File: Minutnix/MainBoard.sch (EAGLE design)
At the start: 134 parts, among them IC1 MEGA8-AI, IC6 TP4056, IC7 FT232RL, IC9 SC4503, Q4 32.768kHz, T1 DMN3024LSD, X1 FH12-12S-0.5SH, X2 JST-XH-03-PIN-LONG-PAD, X4 JST-XH-03-PIN-LONG-PAD

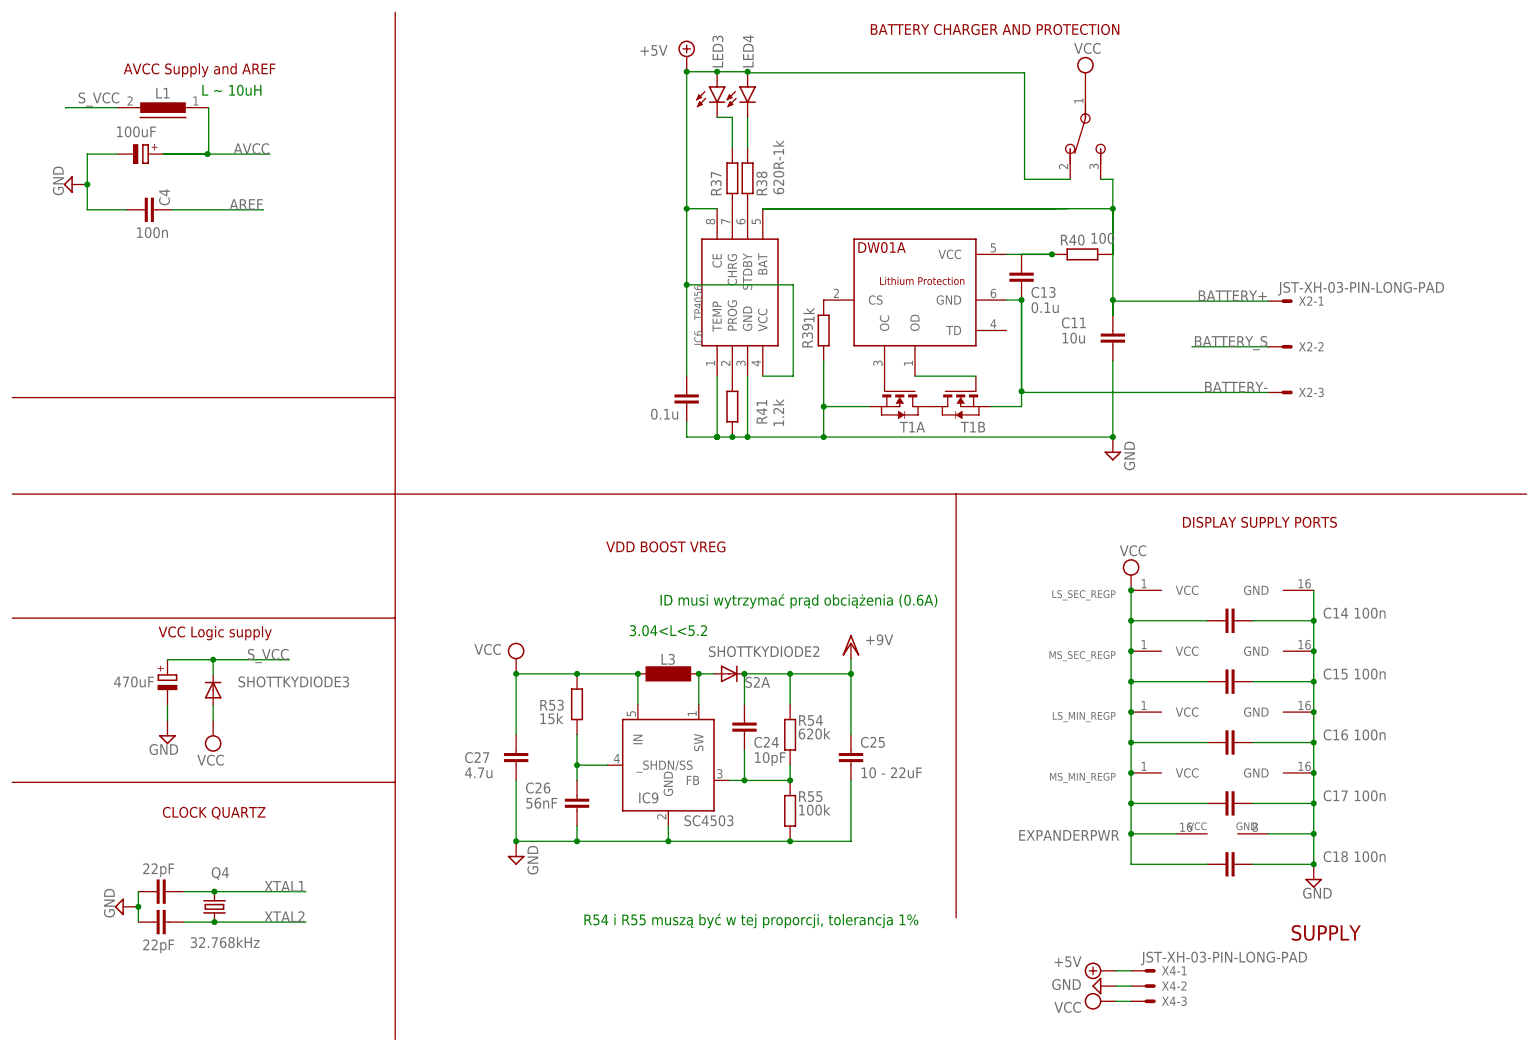
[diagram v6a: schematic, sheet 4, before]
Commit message: Supply replacements + corrections
Vreg replaced by pololu board
Added LDO for VCC supply and moved power on switch
Protection included into battery cicruit
Corrected supply of ft232 diodes
Changed supply of photoresistor to avcc
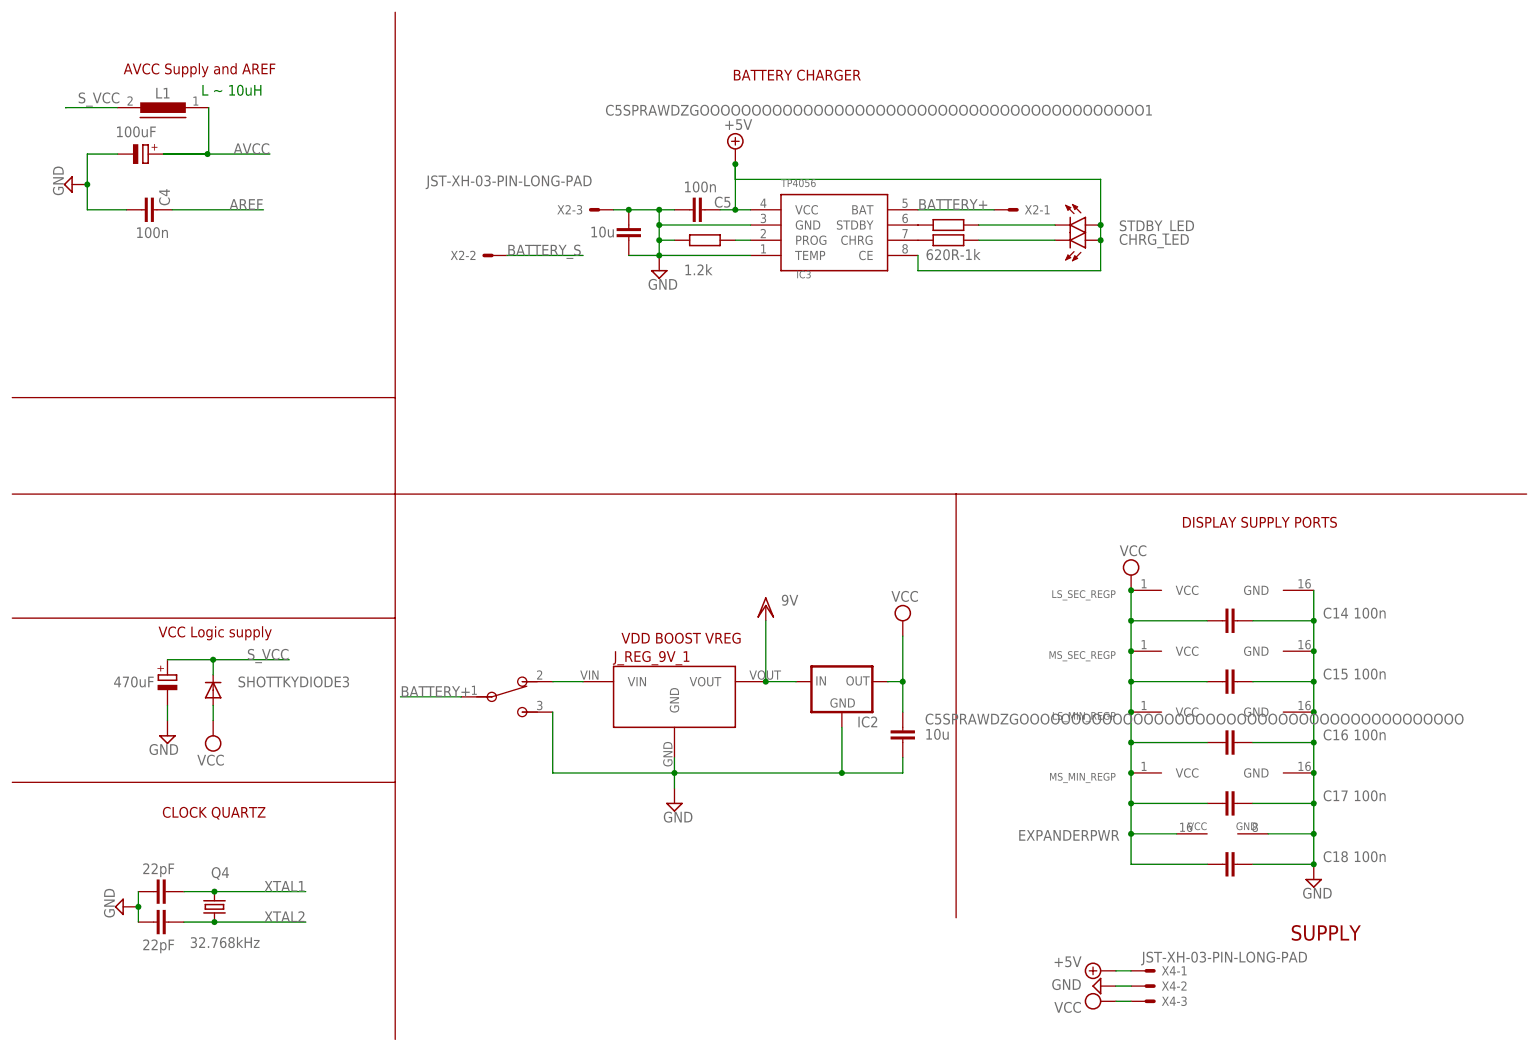
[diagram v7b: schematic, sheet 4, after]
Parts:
- removed C11: 10u, capacitor-wima:C2.5/2
- removed C12, C13: 0.1u, capacitor-wima:C2.5/2
- removed C24: 10pF, capacitor-wima:C2.5/2
- removed C25: 10 - 22uF, capacitor-wima:C2.5/2
- removed C26: 56nF, capacitor-wima:C2.5/2
- removed C27: 4.7u, capacitor-wima:C2.5/2
- removed IC6: TP4056, TP4056:TP4056
- removed IC9: SC4503, v-reg-3:SC4503
- removed L3: 4.237H, inductor-neosid:MS42
- removed LED3, LED4: (no value), led:LEDCHIPLED_0603
- removed R37: 620R-1K, rcl:R-EU_R1206
- removed R38: 620R-1k, rcl:R-EU_R1206
- removed R41: 1.2k, rcl:R-EU_R1206
- removed R53: 15k, rcl:R-EU_R1206
- removed R54: 620k, rcl:R-EU_R1206
- removed R55: 100k, rcl:R-EU_R1206
- removed SHOTTKYDIODE2: S2A, s2x_10:S2A
- removed T1: DMN3024LSD, FS8205A:DMN3024LSD
- removed U$2: DW01A, DW01A:DW01A
- added C5: 100n, rcl:C-EUC0603
- added C5SPRAWDZGOOOOOOOOOOOOOOOOOOOOOOOOOOOOOOOOOOOOOOOOOOO, C5SPRAWDZGOOOOOOOOOOOOOOOOOOOOOOOOOOOOOOOOOOOOOOOOOOO1: 10u, rcl:C-EUC3216
- added CHRG_LED, STDBY_LED: (no value), led:LEDCHIPLED_0603
- added IC2: (no value), v-reg-2:LM1117
- added IC3: TP4056, TP4056:TP4056
- added J_REG_9V_1: 9V_VOLTAGE_REGULATOR, Pololu_vreg:9V_VOLTAGE_REGULATOR
- added R48: 1.2k, rcl:R-EU_R0603
- R39: value 1k -> 620R-1k; device rcl:R-EU_R1206 -> rcl:R-EU_R0603
- R40: value 100 -> 620R-1k; device rcl:R-EU_R1206 -> rcl:R-EU_R0603
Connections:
- removed net BATTERY-: C13.1, T1B.S, U$2.GND, X2-3.S
- removed net N$100: LED3.C, R37.2
- removed net N$101: LED4.C, R38.2
- removed net N$102: T1A.G, U$2.OC
- removed net N$104: T1A.D, T1B.D
- removed net N$105: T1B.G, U$2.OD
- removed net N$106: R39.2, U$2.CS
- removed net N$109: C13.2, R40.2, U$2.VCC
- removed net N$111: IC6.PROG, R41.2
- removed net N$113: IC9.SW, L3.1, SHOTTKYDIODE2.A
- removed net N$118: C26.2, IC9._SHDN/SS, R53.2
- removed net N$119: C24.1, IC9.FB, R54.2, R55.1
- removed net N$98: IC6.CHRG, R37.1
- removed net N$99: IC6.STDBY, R38.1
- new net N$29: J_REG_9V_1.VIN, U$1.2
- new net N$52: IC3.CHRG, R39.2
- new net N$53: IC3.STDBY, R40.2
- new net N$54: CHRG_LED.C, R39.1
- new net N$55: R40.1, STDBY_LED.C
- new net N$82: IC3.PROG, R48.1
- new net N$84: RXLED.A, TXLED.A
- net +3V3: no longer RXLED.A, TXLED.A
- net +5V: now also C5.1, CHRG_LED.A, IC3.CE, IC3.VCC, STDBY_LED.A; no longer C12.2, IC6.CE, IC6.VCC, LED3.A, LED4.A, U$1.2
- net AVCC: now also R57.A
- net BATTERY+: now also IC3.BAT, U$1.1; no longer C11.2, IC6.BAT, R40.1, U$1.3
- net GND: now also C5.2, C5SPRAWDZGOOOOOOOOOOOOOOOOOOOOOOOOOOOOOOOOOOOOOOOOOOO.2, C5SPRAWDZGOOOOOOOOOOOOOOOOOOOOOOOOOOOOOOOOOOOOOOOOOOO1.1, C5SPRAWDZGOOOOOOOOOOOOOOOOOOOOOOOOOOOOOOOOOOOOOOOOOOO1.2, IC2.GND, IC3.GND, IC3.TEMP, J_REG_9V_1.GND, R48.2, U$1.3, X2-3.S; no longer C11.1, C12.1, C25.1, C26.1, C27.1, IC6.GND, IC6.TEMP, IC9.GND, R39.1, R41.1, R55.2, T1A.S
- net VCC: now also C5SPRAWDZGOOOOOOOOOOOOOOOOOOOOOOOOOOOOOOOOOOOOOOOOOOO.1, IC2.OUT; no longer C27.2, IC9.IN, L3.2, R53.1, U$1.1
- net VDD: now also IC2.IN, J_REG_9V_1.VOUT; no longer C24.2, C25.2, R54.1, R57.A, SHOTTKYDIODE2.C
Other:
- note added: "BATTERY CHARGER"
- note removed: "3.04<L<5.2"
- note removed: "BATTERY CHARGER AND PROTECTION"
- note removed: "ID musi wytrzymać prąd obciążenia (0.6A)"
- note removed: "R54 i R55 muszą być w tej proporcji, tolerancja 1%"
- moved on the sheet: X2-1, X2-2, X2-3

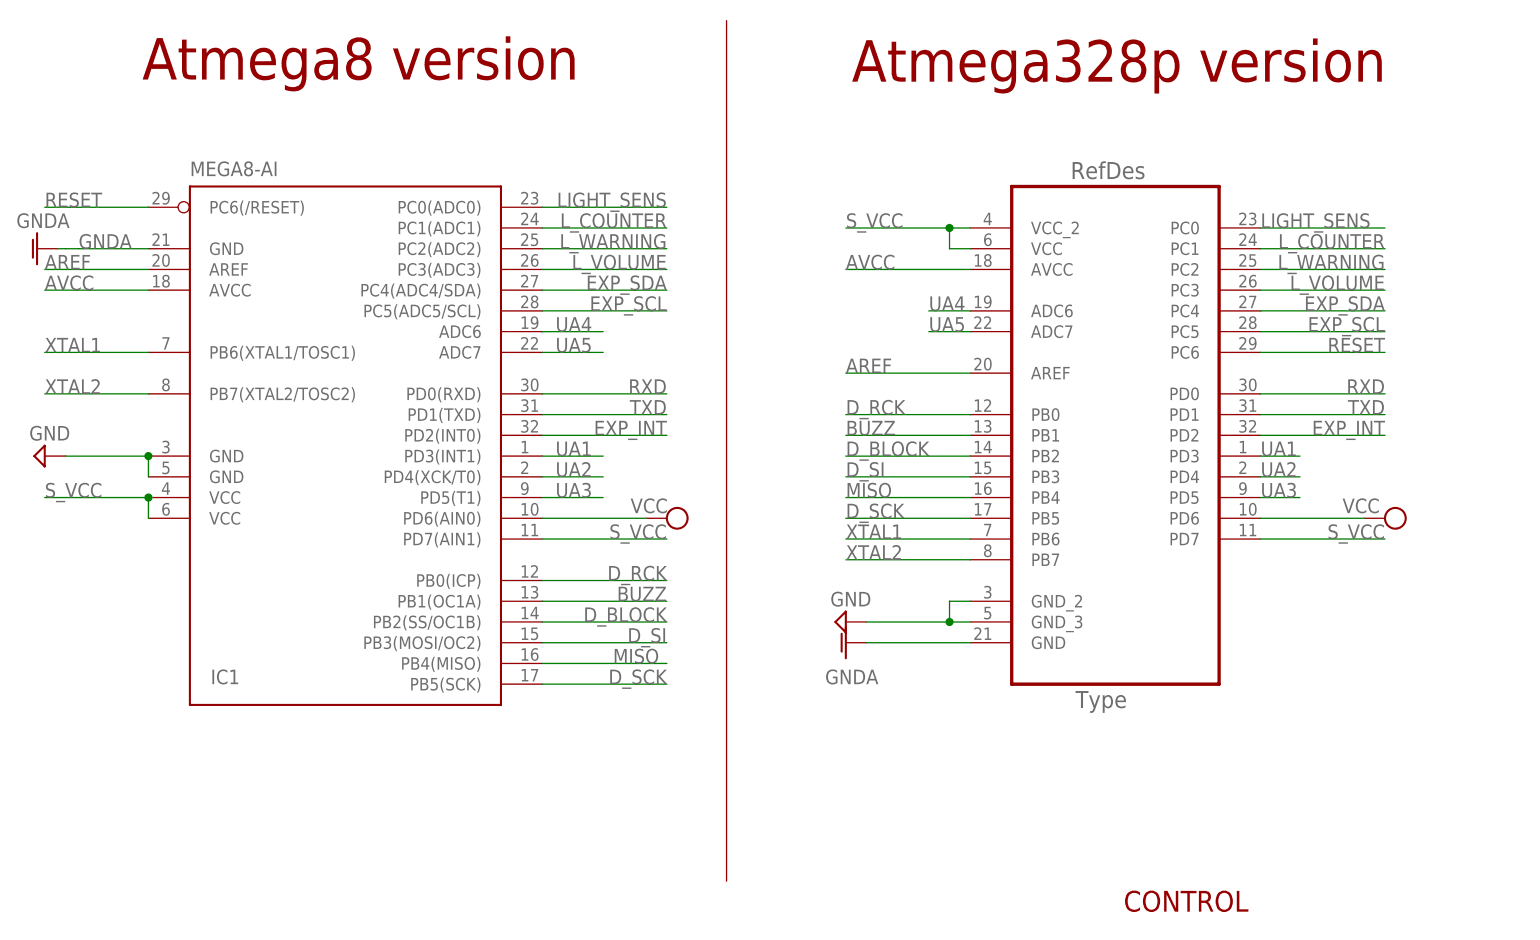
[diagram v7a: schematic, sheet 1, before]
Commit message: 7segm lib + board
Corrections on consistency and erc errors
readded 7 segm. custom lib
Partial components placement and routing tries
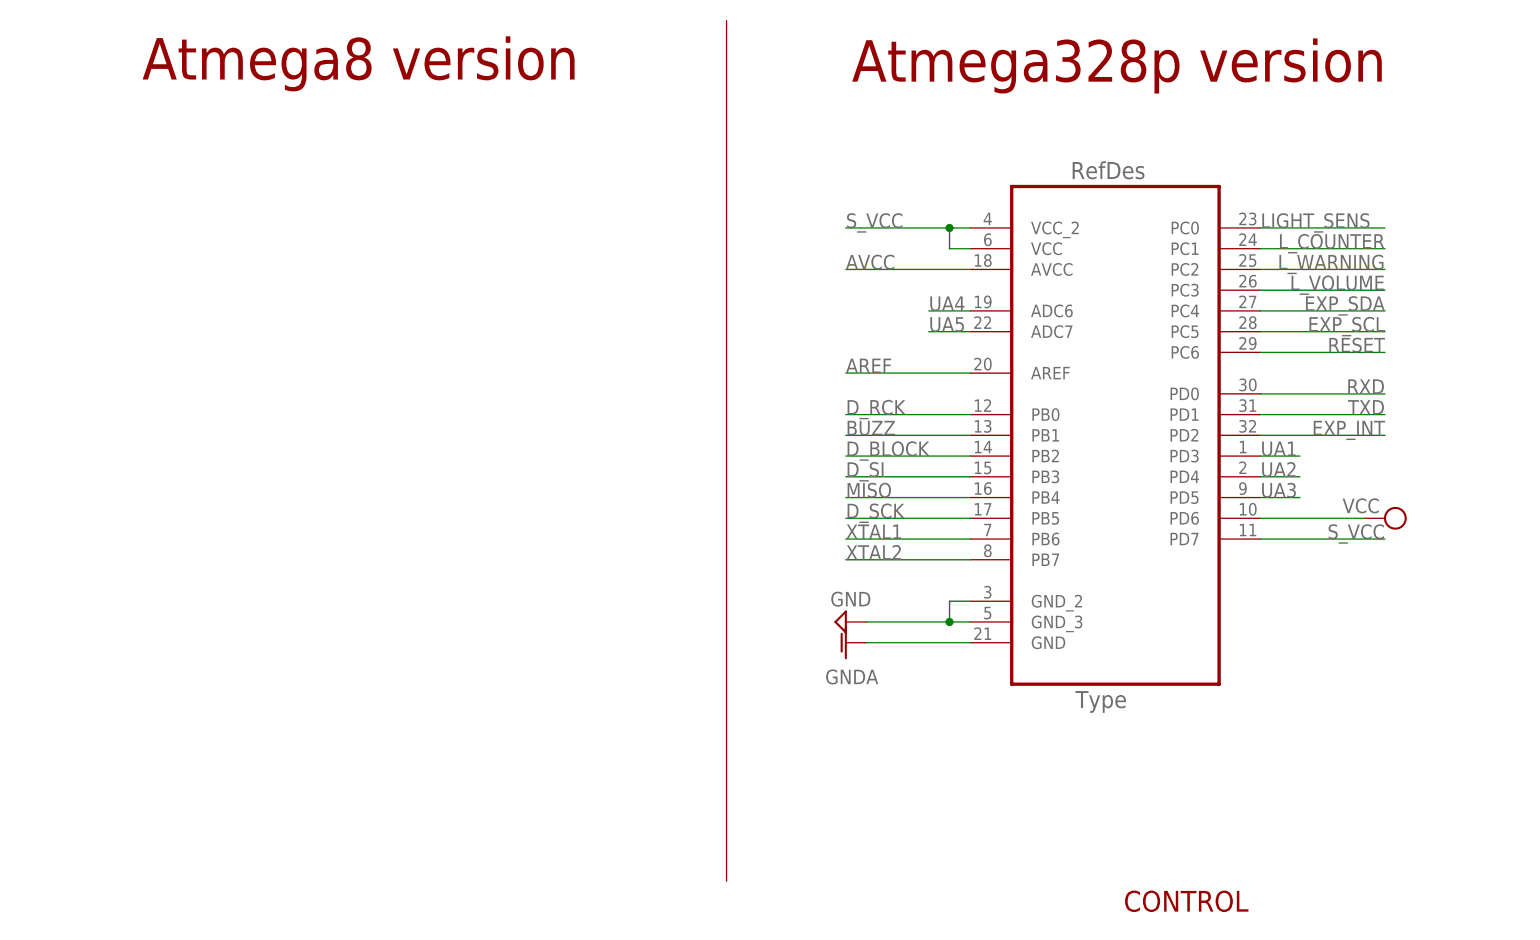
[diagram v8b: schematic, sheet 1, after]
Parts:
- removed IC1: MEGA8-AI, atmel:MEGA8-AI
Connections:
- net +3V3 renamed N$27
- removed net DI: JP16.1
- removed net N$84: RXLED.A, TXLED.A
- removed net VDD1: LSDIGIT_MINUTES.CA1, LSDIGIT_MINUTES.CA8, LSDIGIT_SECONDS.CA1, LSDIGIT_SECONDS.CA8, MSDIGIT_MINUTES.CA1, MSDIGIT_MINUTES.CA8, MSDIGIT_SECONDS.CA1, MSDIGIT_SECONDS.CA8
- net +5V: now also RXLED.A, TXLED.A
- net AREF: no longer IC1.AREF
- net AVCC: no longer IC1.AVCC
- net BUZZ: no longer IC1.PB1(OC1A)
- net D_BLOCK: no longer IC1.PB2(SS/OC1B)
- net D_RCK: no longer IC1.PB0(ICP)
- net D_SCK: no longer IC1.PB5(SCK)
- net D_SI: no longer IC1.PB3(MOSI/OC2)
- net EXP_INT: no longer IC1.PD2(INT0)
- net EXP_SCL: no longer IC1.PC5(ADC5/SCL)
- net EXP_SDA: no longer IC1.PC4(ADC4/SDA)
- net GND: no longer IC1.GND@1, IC1.GND@2
- net GNDA: no longer IC1.GND
- net LIGHT_SENS: no longer IC1.PC0(ADC0)
- net L_COUNTER: no longer IC1.PC1(ADC1)
- net L_VOLUME: no longer IC1.PC3(ADC3)
- net L_WARNING: no longer IC1.PC2(ADC2)
- net MISO: no longer IC1.PB4(MISO)
- net RESET: no longer IC1.PC6(/RESET)
- net RI: now also JP16.1
- net RXD: no longer IC1.PD0(RXD)
- net S_VCC: no longer IC1.PD7(AIN1), IC1.VCC@1, IC1.VCC@2
- net TXD: no longer IC1.PD1(TXD)
- net UA1: no longer IC1.PD3(INT1)
- net UA2: no longer IC1.PD4(XCK/T0)
- net UA3: no longer IC1.PD5(T1)
- net UA4: no longer IC1.ADC6
- net UA5: no longer IC1.ADC7
- net VCC: no longer IC1.PD6(AIN0)
- net VDD: now also LSDIGIT_MINUTES.CA1, LSDIGIT_MINUTES.CA8, LSDIGIT_SECONDS.CA1, LSDIGIT_SECONDS.CA8, MSDIGIT_MINUTES.CA1, MSDIGIT_MINUTES.CA8, MSDIGIT_SECONDS.CA1, MSDIGIT_SECONDS.CA8
- net XTAL1: no longer IC1.PB6(XTAL1/TOSC1)
- net XTAL2: no longer IC1.PB7(XTAL2/TOSC2)
